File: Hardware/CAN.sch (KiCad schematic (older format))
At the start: 10 parts, among them U3 ATA6561-GAQW-N

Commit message: power
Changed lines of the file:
@@
 AR Path="/61A14ADD/61A168ED" Ref="U3"  Part="1"
 AR Path="/61A9D384/61A168ED" Ref="U4"  Part="1"
-AR Path="/61B35764/61A168ED" Ref="U4"  Part="1"
-F 0 "U4" H 6100 4450 50  0000 C CNN
+AR Path="/61B35764/61A168ED" Ref="U3"  Part="1"
+F 0 "U3" H 6100 4450 50  0000 C CNN
 F 1 "ATA6561-GAQW-N" H 6200 4350 50  0000 C CNN
 F 2 "Package_DFN_QFN:DFN-8-1EP_3x3mm_P0.65mm_EP1.55x2.4mm" H 5700 3450 50  0001 C CIN

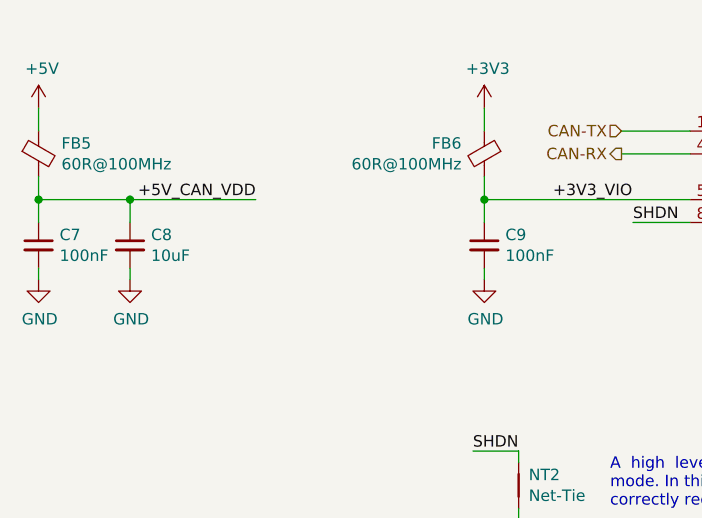
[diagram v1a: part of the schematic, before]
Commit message: uC supply added
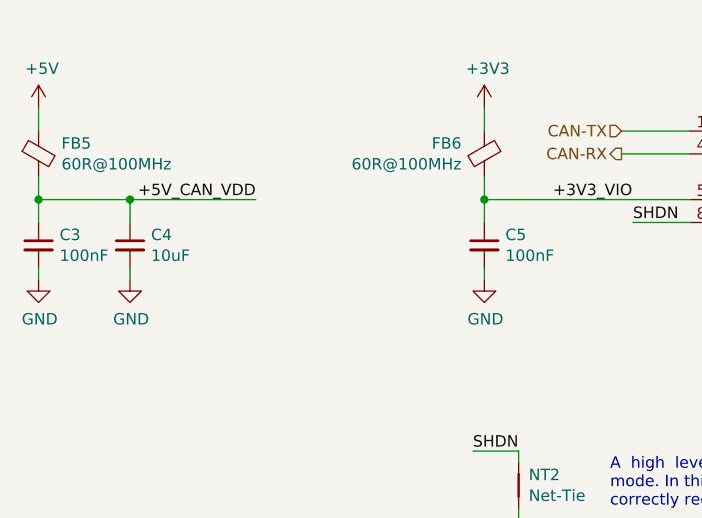
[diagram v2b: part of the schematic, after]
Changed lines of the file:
@@
 AR Path="/61A14ADD/61A25B3D" Ref="C6"  Part="1"
 AR Path="/61A9D384/61A25B3D" Ref="C9"  Part="1"
-AR Path="/61B35764/61A25B3D" Ref="C9"  Part="1"
-F 0 "C9" H 4392 4296 50  0000 L CNN
+AR Path="/61B35764/61A25B3D" Ref="C5"  Part="1"
+F 0 "C5" H 4392 4296 50  0000 L CNN
 F 1 "100nF" H 4392 4205 50  0000 L CNN
 F 2 "" H 4300 4250 50  0001 C CNN
@@
 AR Path="/61A14ADD/61AA448F" Ref="C4"  Part="1"
 AR Path="/61A9D384/61AA448F" Ref="C7"  Part="1"
-AR Path="/61B35764/61AA448F" Ref="C7"  Part="1"
-F 0 "C7" H 2442 4296 50  0000 L CNN
+AR Path="/61B35764/61AA448F" Ref="C3"  Part="1"
+F 0 "C3" H 2442 4296 50  0000 L CNN
 F 1 "100nF" H 2442 4205 50  0000 L CNN
 F 2 "" H 2350 4250 50  0001 C CNN
@@
 AR Path="/61A14ADD/61AAD0CE" Ref="C5"  Part="1"
 AR Path="/61A9D384/61AAD0CE" Ref="C8"  Part="1"
-AR Path="/61B35764/61AAD0CE" Ref="C8"  Part="1"
-F 0 "C8" H 2842 4296 50  0000 L CNN
+AR Path="/61B35764/61AAD0CE" Ref="C4"  Part="1"
+F 0 "C4" H 2842 4296 50  0000 L CNN
 F 1 "10uF" H 2842 4205 50  0000 L CNN
 F 2 "" H 2750 4250 50  0001 C CNN

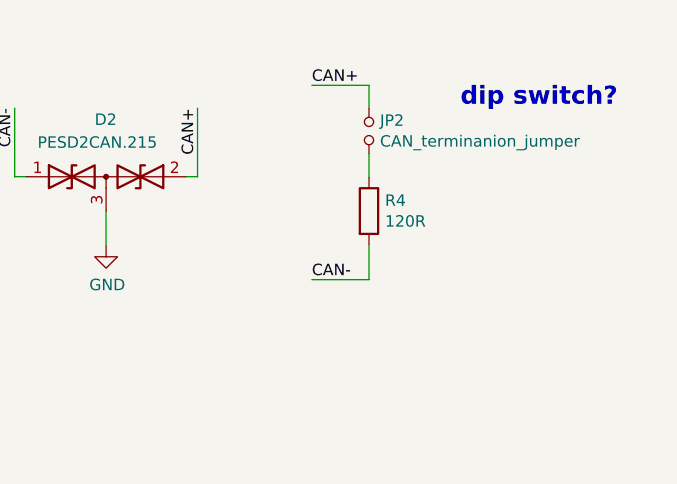
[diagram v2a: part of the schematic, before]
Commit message: added reset button
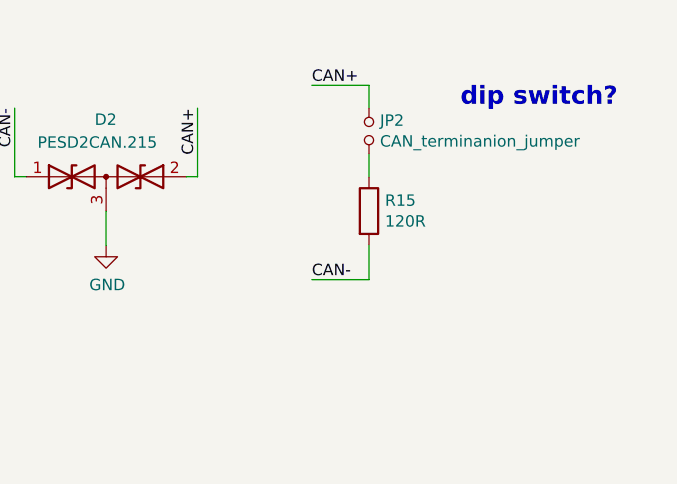
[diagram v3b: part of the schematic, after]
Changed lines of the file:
@@
 AR Path="/61A14ADD/61A896F4" Ref="R3"  Part="1"
 AR Path="/61A9D384/61A896F4" Ref="R4"  Part="1"
-AR Path="/61B35764/61A896F4" Ref="R4"  Part="1"
-F 0 "R4" H 8970 4146 50  0000 L CNN
+AR Path="/61B35764/61A896F4" Ref="R15"  Part="1"
+F 0 "R15" H 8970 4146 50  0000 L CNN
 F 1 "120R" H 8970 4055 50  0000 L CNN
 F 2 "" V 8830 4100 50  0001 C CNN

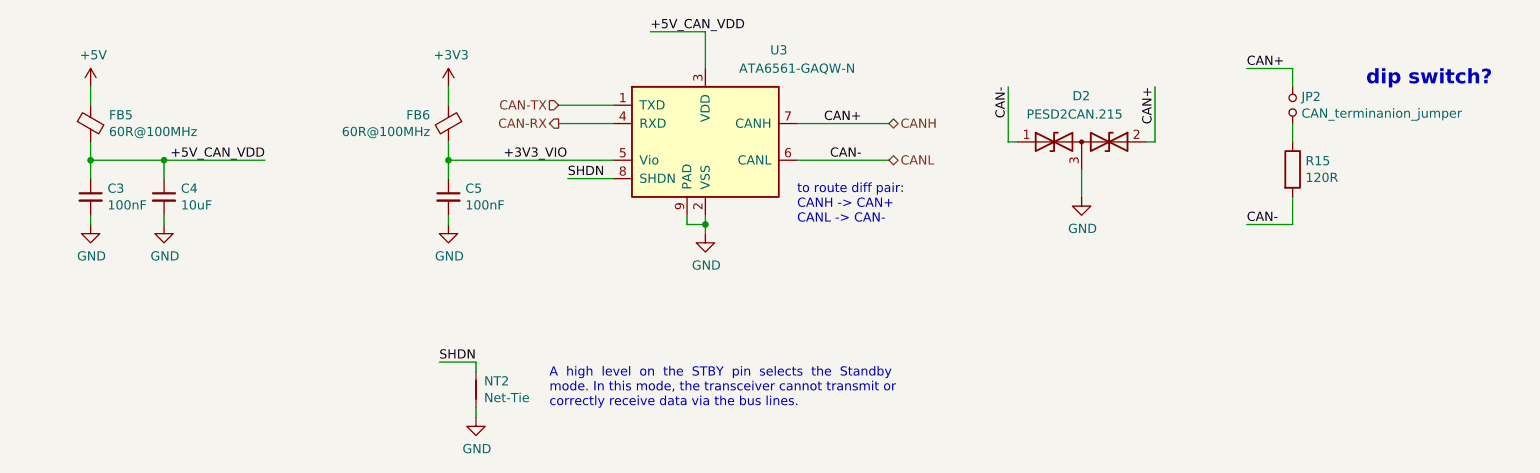
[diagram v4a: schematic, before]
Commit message: added footprints, updated CAN, annotated symbols
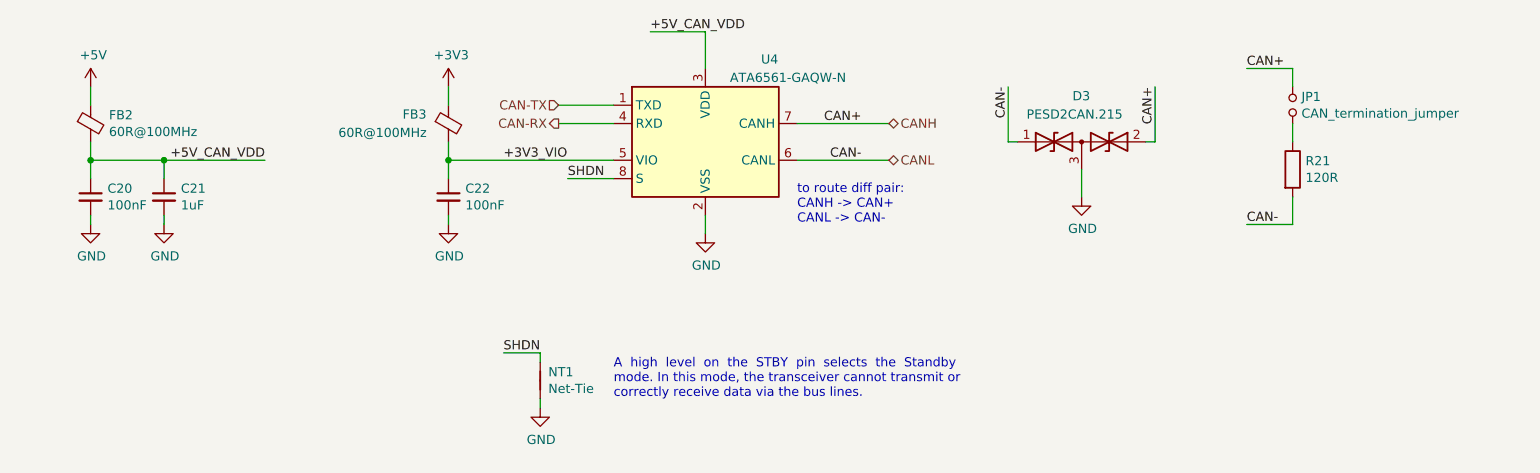
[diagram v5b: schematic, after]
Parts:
- removed FB4: 60R@100MHz, Inductor_SMD:L_0603_1608Metric, symbol Device:Ferrite_Bead_Small
- removed U3: ATA6561-GAQW-N, Package_DFN_QFN:DFN-8-1EP_3x3mm_P0.65mm_EP1.55x2.4mm, symbol Interface_CAN_LIN:MCP2562-E-MF
- added FB3: 60R@100MHz, Inductor_SMD:L_0603_1608Metric, symbol Device:Ferrite_Bead_Small
- added U4: ATA6561-GAQW-N, Package_SO:SOIC-8_3.9x4.9mm_P1.27mm, symbol Interface_CAN_LIN:MCP2558FD-xSN
- C20: renamed from C4; footprint (none) -> Capacitor_SMD:C_0603_1608Metric
- C21: renamed from C5; value 10uF -> 1uF; footprint (none) -> Capacitor_SMD:C_0603_1608Metric
- C22: renamed from C6; footprint (none) -> Capacitor_SMD:C_0603_1608Metric
- JP1: value CAN_terminanion_jumper -> CAN_termination_jumper
- NT1: footprint (none) -> NetTie:NetTie-2_SMD_Pad0.5mm
- R21: renamed from R3; footprint (none) -> Resistor_SMD:R_0603_1608Metric
- renumbered D12 to D3
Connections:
- net +3V3: now also FB3.1
- net +3V3_VIO: now also FB3.2, U4.5 (VIO)
- net +5V_CAN_VDD: now also U4.3 (VDD)
- net CAN-RX: now also U4.4 (RXD)
- net CAN-TX: now also U4.1 (TXD)
- net CANH: now also U4.7 (CANH)
- net CANL: now also U4.6 (CANL)
- net GND: now also U4.2 (VSS)
- net SHDN: now also U4.8 (S)
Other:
- note removed: "dip switch?"
- moved on the sheet: NT1

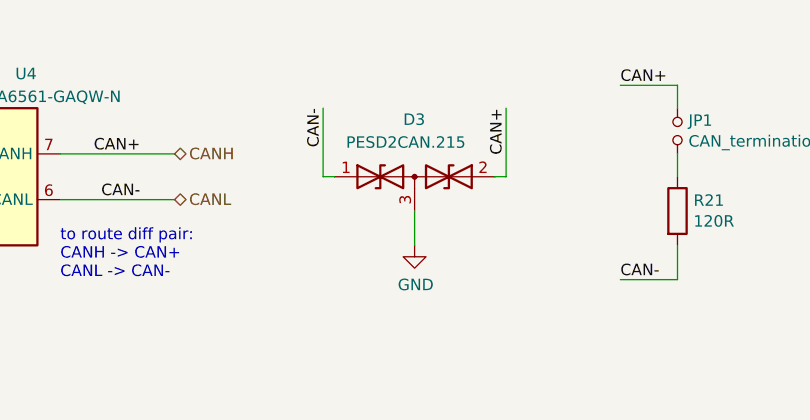
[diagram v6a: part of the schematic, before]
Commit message: added button for starting procedure, changes to pcb layout pending
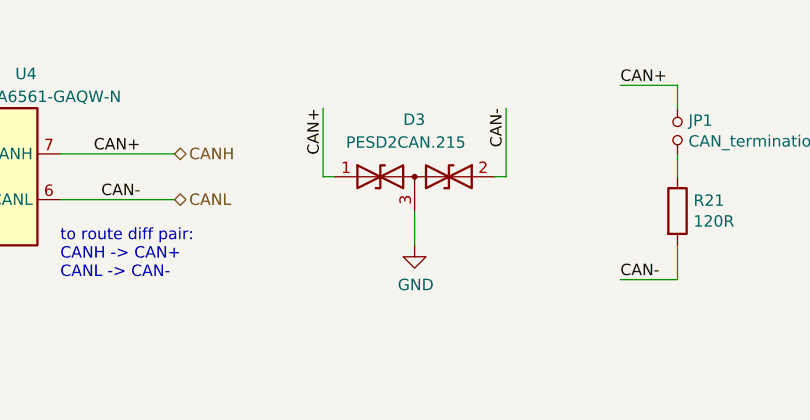
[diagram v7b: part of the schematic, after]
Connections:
- net CANH: now also D3.1 (A1); no longer D3.2 (A2)
- net CANL: now also D3.2 (A2); no longer D3.1 (A1)
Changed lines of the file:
@@
 $Descr A4 11693 8268
 encoding utf-8
-Sheet 3 7
+Sheet 3 8
 Title "CAN"
 Date ""
@@
 	7400 3950 7350 3950
 Wire Wire Line
-	7350 3950 7350 3650
+	8150 3950 8150 3650
 Wire Wire Line
 	8100 3950 8150 3950
 Wire Wire Line
-	8150 3950 8150 3650
+	7350 3950 7350 3650
 Wire Wire Line
 	7750 4250 7750 4100
@@
 Text Notes 6200 4400 0    50   ~ 0
 to route diff pair:\nCANH -> CAN+\nCANL -> CAN-\n
+Text Label 8150 3650 3    50   ~ 0
+CAN-
 Text Label 7350 3650 3    50   ~ 0
-CAN-
-Text Label 8150 3650 3    50   ~ 0
 CAN+
 Text Label 8650 4400 0    50   ~ 0

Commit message: updated pcb
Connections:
- net +5V renamed safe5V
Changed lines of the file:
@@
-	1    0    0    -1
-$EndComp
-$Comp
-L power:+5V #PWR?
-U 1 1 61A24688
-P 2350 3650
-AR Path="/61A14ADD/61A24688" Ref="#PWR?"  Part="1"
-AR Path="/61A9D384/61A24688" Ref="#PWR?"  Part="1"
-AR Path="/61B3EE71/61A24688" Ref="#PWR?"  Part="1"
-AR Path="/620E9BA8/61A24688" Ref="#PWR031"  Part="1"
-F 0 "#PWR031" H 2350 3500 50  0001 C CNN
-F 1 "+5V" H 2365 3823 50  0000 C CNN
-F 2 "" H 2350 3650 50  0001 C CNN
-F 3 "" H 2350 3650 50  0001 C CNN
-	1    2350 3650
 	1    0    0    -1
 $EndComp
@@
 Text HLabel 6700 3850 2    50   BiDi ~ 0
 CANH
+Text GLabel 2350 3650 0    50   Input ~ 0
+safe5V
 $EndSCHEMATC
